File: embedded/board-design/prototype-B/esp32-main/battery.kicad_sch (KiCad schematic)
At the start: 14 parts, among them J7 Conn_01x02_Socket, J8 Conn_01x03_Socket, Q6 FDN340P, Q7 FDN340P, U5 LTC4054ES5-4.2

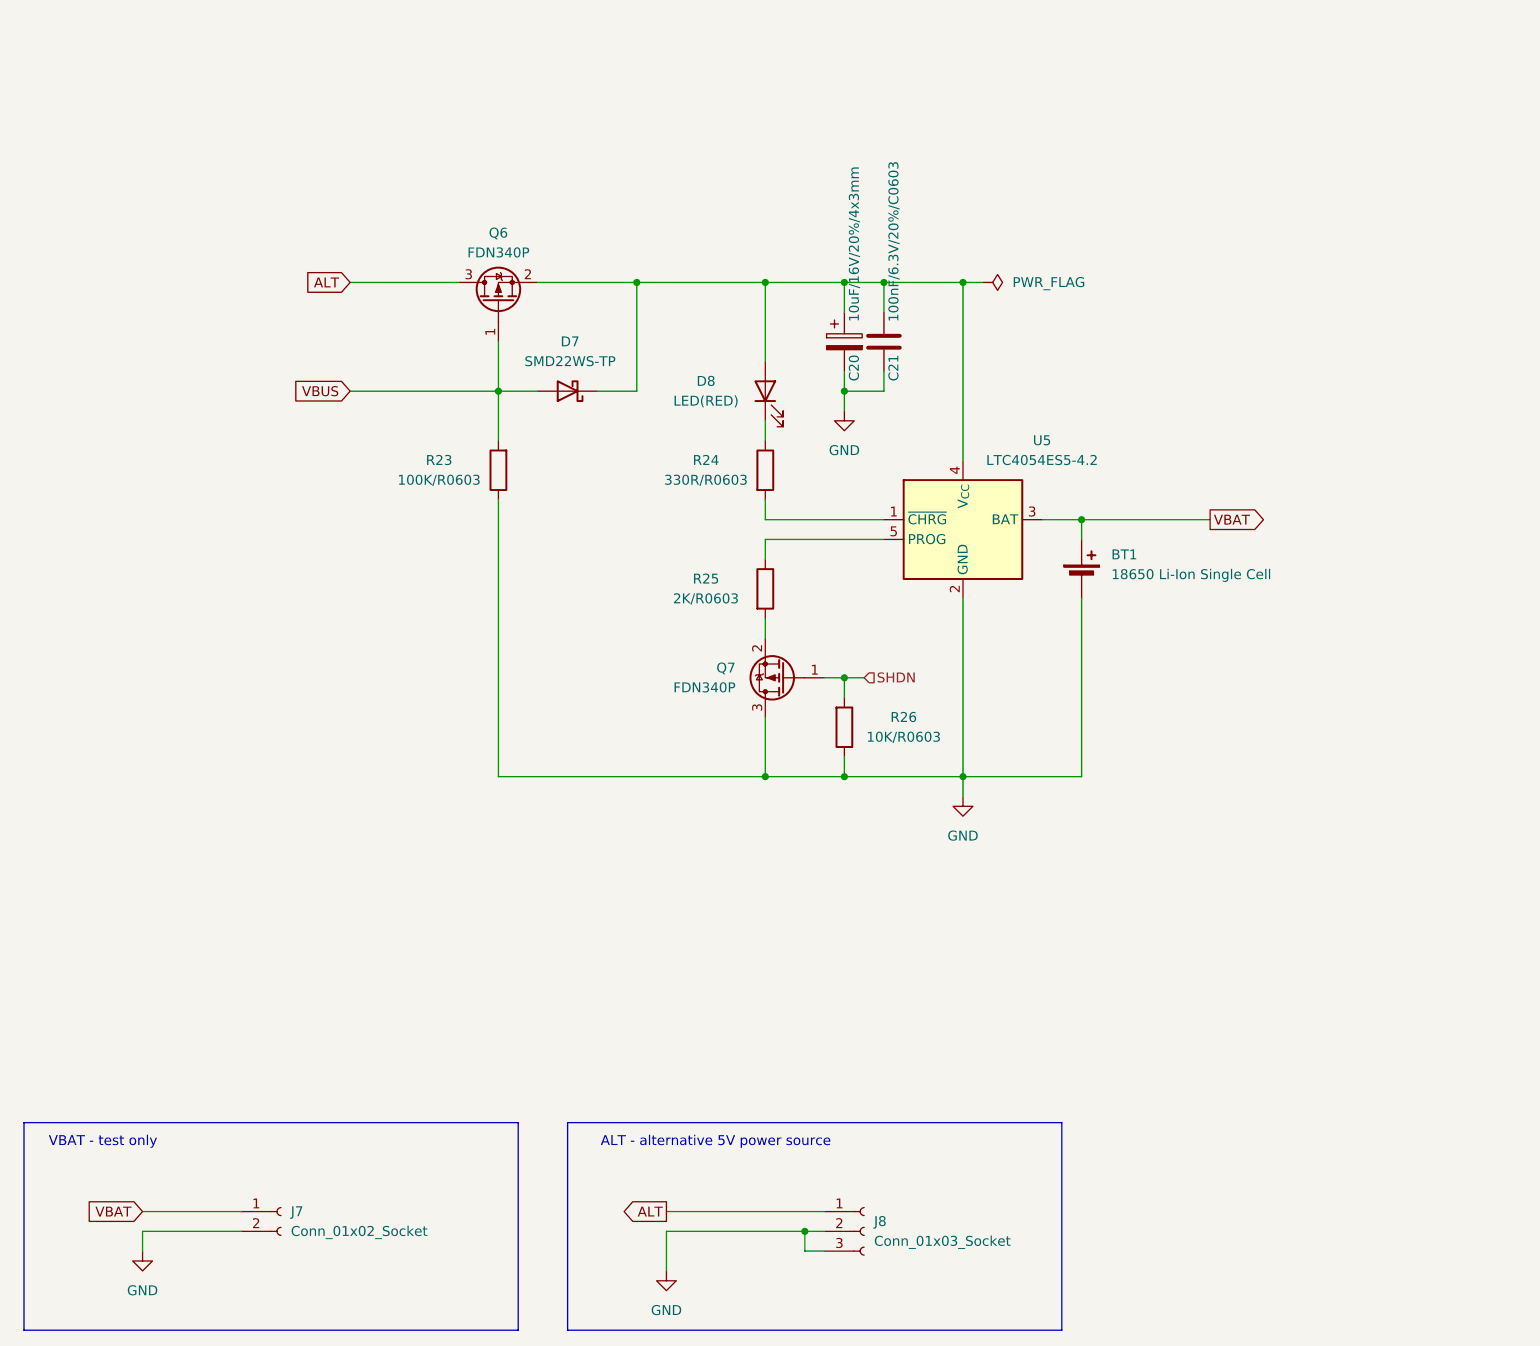
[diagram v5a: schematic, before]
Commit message: [prototype-B]
Refactored hardware implementation. Reduced board size.

Signed-off-by: Nicolae-Andrei Vasile <vasilenicolaeandrei@gmail.com>
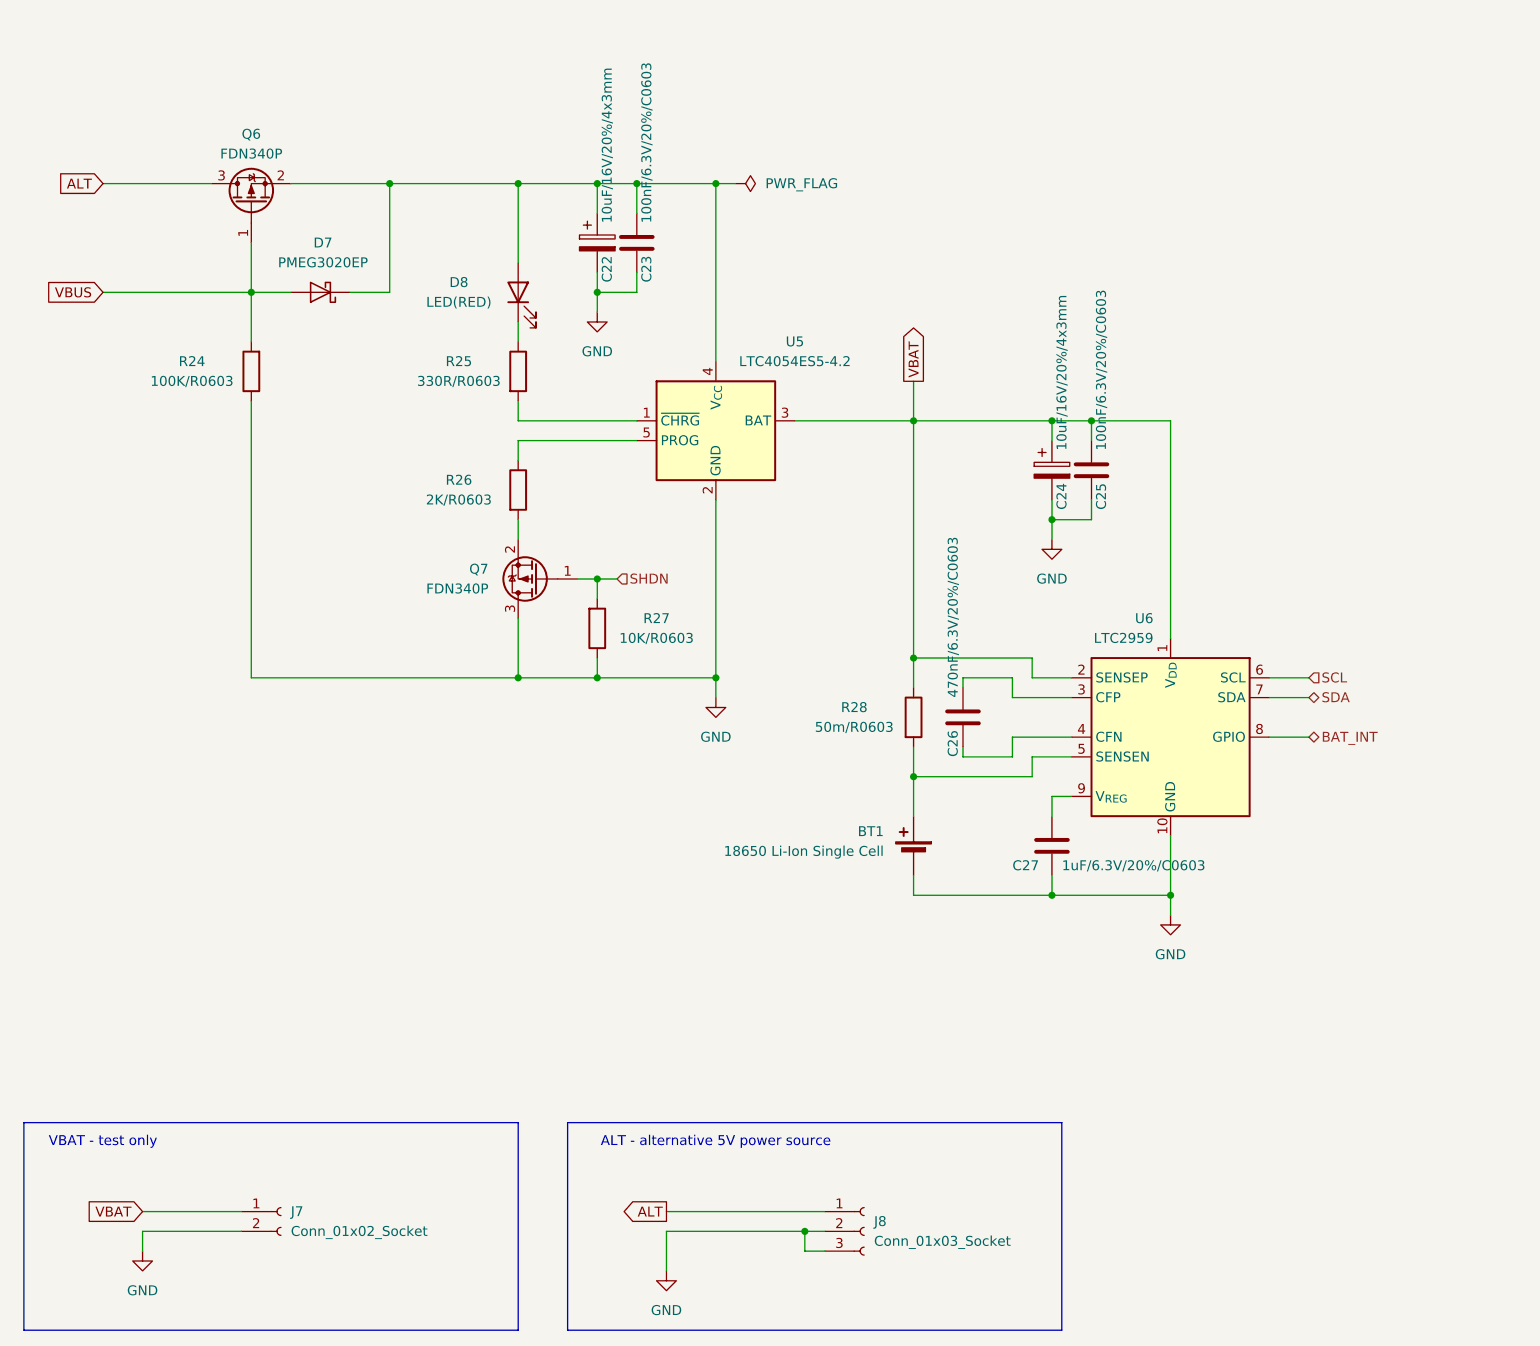
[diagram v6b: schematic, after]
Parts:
- removed D7: SMD22WS-TP, Diode_SMD:D_SOD-323_HandSoldering, symbol Device:D_Schottky
- added C24: 10uF/16V/20%/4x3mm, Capacitor_SMD:CP_Elec_4x3, symbol Device:C_Polarized
- added C25: 100nF/6.3V/20%/C0603, Capacitor_SMD:C_0603_1608Metric_Pad1.08x0.95mm_HandSolder, symbol Device:C
- added C26: 470nF/6.3V/20%/C0603, Capacitor_SMD:C_0603_1608Metric_Pad1.08x0.95mm_HandSolder, symbol Device:C
- added C27: 1uF/6.3V/20%/C0603, Capacitor_SMD:C_0603_1608Metric_Pad1.08x0.95mm_HandSolder, symbol Device:C
- added D7: PMEG3020EP, Diode_SMD:D_SOD-128, symbol Diode:PMEG3020ER
- added R28: 50m/R0603, Resistor_SMD:R_0603_1608Metric_Pad0.98x0.95mm_HandSolder, symbol Device:R
- added U6: LTC2959, Package_DFN_QFN:DFN-10-1EP_2x3mm_P0.5mm_EP0.64x2.4mm, symbol Battery_Management:LTC2959
- J7: footprint Connector_PinHeader_1.27mm:PinHeader_1x02_P1.27mm_Vertical -> Connector_PinHeader_2.54mm:PinHeader_1x02_P2.54mm_Vertical
- J8: footprint Connector_Phoenix_MC:PhoenixContact_MC_1,5_3-G-3.81_1x03_P3.81mm_Horizontal -> TerminalBlock_Phoenix:TerminalBlock_Phoenix_MPT-0,5-3-2.54_1x03_P2.54mm_Horizontal
- renumbered C20 to C22, C21 to C23, R23 to R24, R24 to R25, R25 to R26, R26 to R27
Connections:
- net GND: now also C24.2, C25.2, C27.2, U6.10 (GND)
- net VBAT: now also C24.1, C25.1, R28.1, U6.1 (V_{DD}), U6.2 (SENSEP); no longer BT1.1 (+)
- net VBUS: now also D7.2 (A)
- net at C22.1, C23.1, D8.2 (A)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: now also D7.1 (K)
- new net: C27.1, U6.9 (V_{REG})
- new net: C26.1, U6.3 (CFP)
- new net: C26.2, U6.4 (CFN)
- new net: BT1.1 (+), R28.2, U6.5 (SENSEN)
- new net BAT_INT: U6.8 (GPIO)
- new net SCL: U6.6 (SCL)
- new net SDA: U6.7 (SDA)
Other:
- moved on the sheet: BT1, C22, C23, D8, Q6, Q7, R24, R25, R26, R27, U5
